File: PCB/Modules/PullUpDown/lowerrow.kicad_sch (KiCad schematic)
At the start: 2 parts

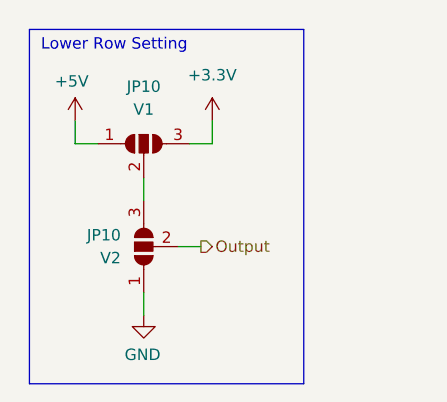
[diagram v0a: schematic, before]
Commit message: Update pull up/down module, with multivoltage ESD protection.
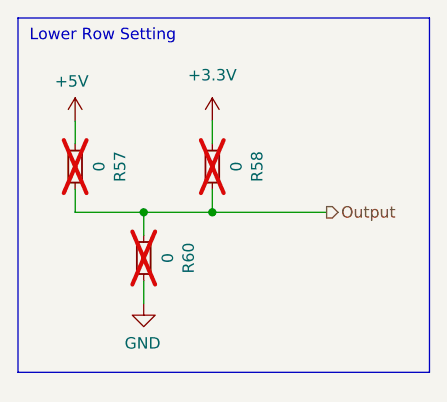
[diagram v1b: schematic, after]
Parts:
- removed JP10: V1, Jumper:SolderJumper-3_P1.3mm_Open_RoundedPad1.0x1.5mm, symbol Jumper:SolderJumper_3_Open
- removed JP10: V2, Jumper:SolderJumper-3_P1.3mm_Open_RoundedPad1.0x1.5mm, symbol Jumper:SolderJumper_3_Open
- added R57, R58, R60: 0, Resistor_SMD:R_0603_1608Metric, symbol Device:R_Small
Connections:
- net +3.3V: now also R58.2
- net +5V: now also R57.2
- net GND: now also R60.1
- net Output: now also R57.1, R58.1, R60.2
